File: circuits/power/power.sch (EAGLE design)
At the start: 22 parts

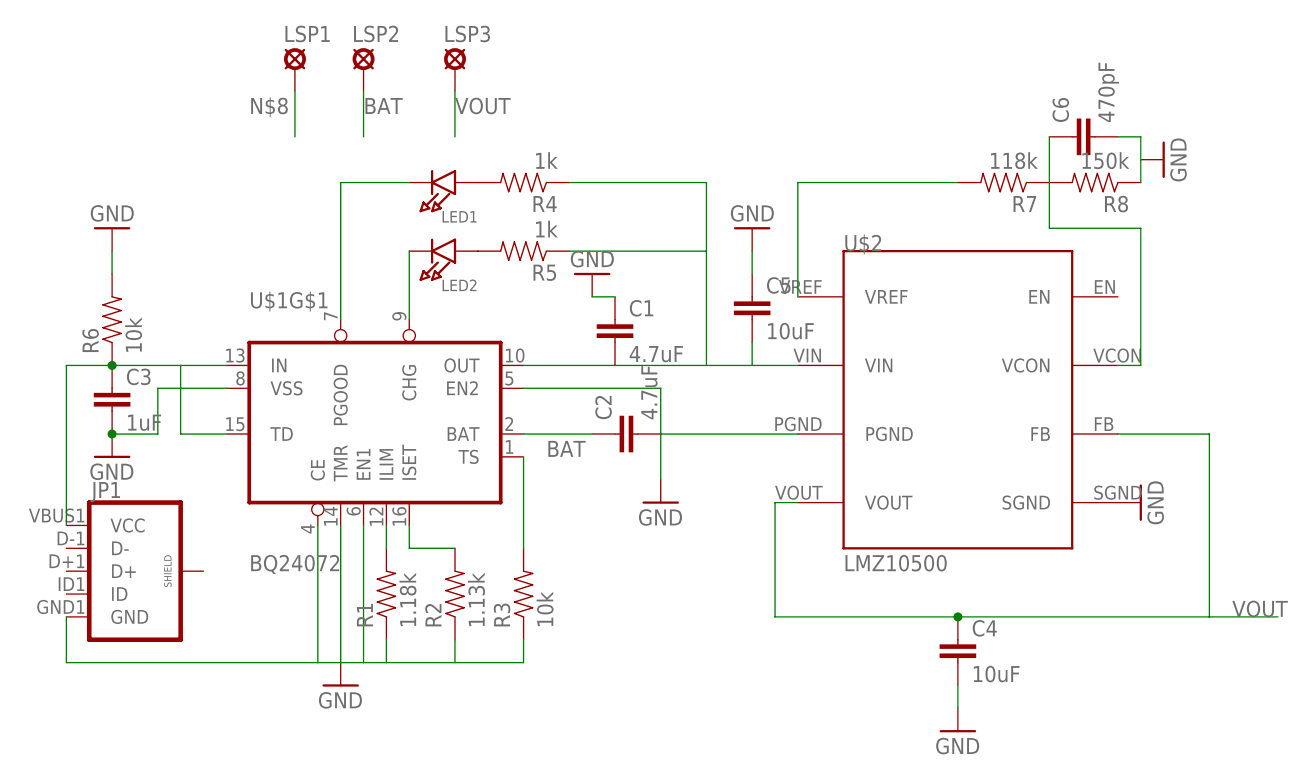
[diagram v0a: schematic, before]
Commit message: changed LMZ10500 library. updated power schematic and switched out usb. Made new power layout.
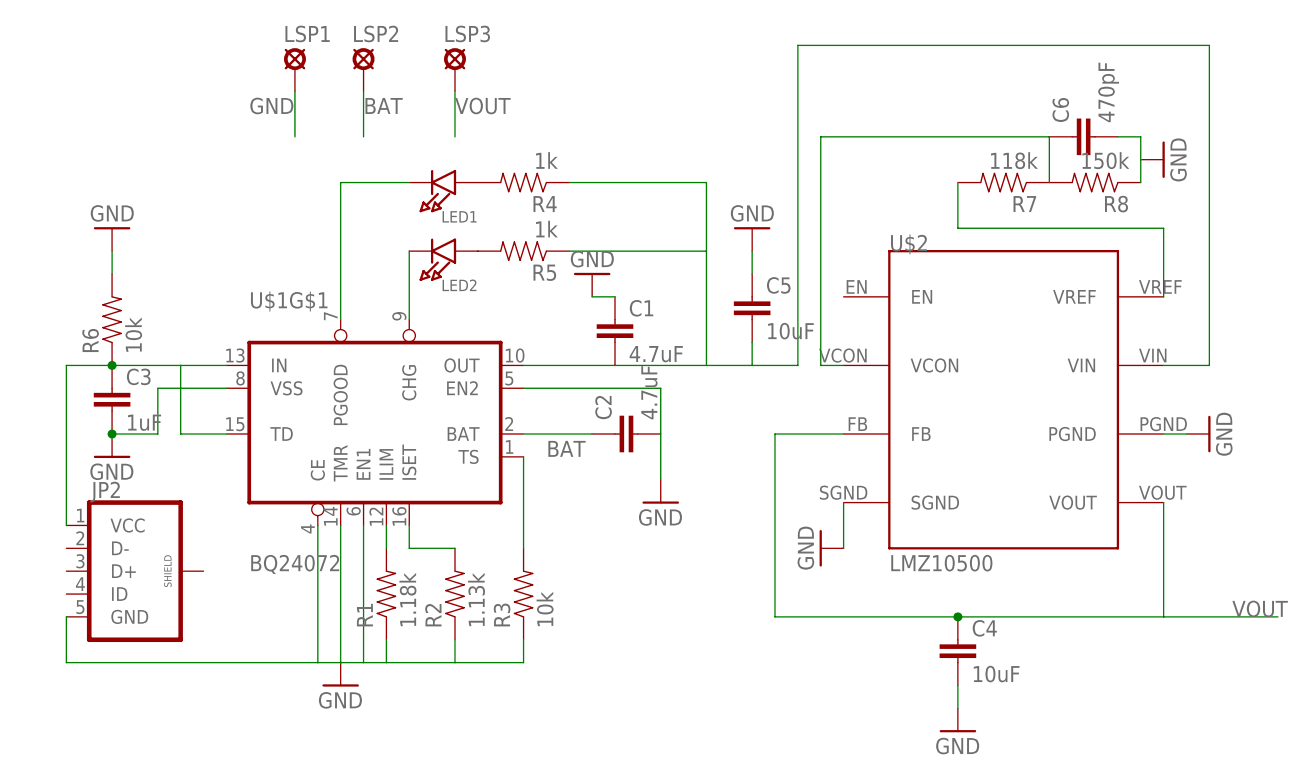
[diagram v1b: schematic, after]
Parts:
- removed JP1: (no value), SparkFun-Connectors:USB_MICROB_PLUGCONN-11752
- added JP2: (no value), SparkFun-Connectors:USB_MICROB_PLUG-SMT
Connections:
- removed net N$25: U$2.SGND
- removed net N$8: C1.1, C2.2, C3.2, C4.2, C5.1, C6.2, JP1.GND, LSP1.MP, R1.1, R2.1, R3.1, R6.2, R8.1, U$1G$1.CE, U$1G$1.EN1, U$1G$1.EN2, U$1G$1.TMR, U$1G$1.VSS, U$2.PGND
- new net GND: C1.1, C2.2, C3.2, C4.2, C5.1, C6.2, JP2.GND, LSP1.MP, R1.1, R2.1, R3.1, R6.2, R8.1, U$1G$1.CE, U$1G$1.EN1, U$1G$1.EN2, U$1G$1.TMR, U$1G$1.VSS, U$2.PGND, U$2.SGND
- net N$14: now also JP2.VCC; no longer JP1.VCC
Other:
- moved on the sheet: U$2
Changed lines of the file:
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@@
 <layer number="112" name="tSilk" color="7" fill="1" visible="yes" active="yes"/>
 <layer number="113" name="IDFDebug" color="4" fill="1" visible="yes" active="yes"/>
+<layer number="114" name="Badge_Outline" color="7" fill="1" visible="yes" active="yes"/>
+<layer number="115" name="ReferenceISLANDS" color="7" fill="1" visible="yes" active="yes"/>
 <layer number="116" name="Patch_BOT" color="9" fill="4" visible="yes" active="yes"/>
 <layer number="118" name="Rect_Pads" color="7" fill="1" visible="yes" active="yes"/>
@@
 <part name="R6" library="SparkFun-Resistors" deviceset="RESISTOR" device="0603" value="10k"/>
 <part name="GND5" library="SparkFun-Aesthetics" deviceset="GND" device=""/>
-<part name="JP1" library="SparkFun-Connectors" deviceset="USB_MICROB_PLUG" device="CONN-11752"/>
 <part name="C4" library="SparkFun-Capacitors" deviceset="CAP" device="0603-CAP" value="10uF"/>
 <part name="C5" library="SparkFun-Capacitors" deviceset="CAP" device="0603-CAP" value="10uF"/>
@@
 <part name="LSP3" library="solpad" deviceset="LSP10" device=""/>
 <part name="U$2" library="LMZ10500" deviceset="LMZ10500" device=""/>
+<part name="GND10" library="SparkFun-Aesthetics" deviceset="GND" device=""/>
+<part name="JP2" library="SparkFun-Connectors" deviceset="USB_MICROB_PLUG" device="-SMT"/>
 </parts>
 <sheets>
@@
 <instance part="R6" gate="G$1" x="63.5" y="63.5" rot="R90"/>
 <instance part="GND5" gate="1" x="63.5" y="73.66" rot="R180"/>
-<instance part="JP1" gate="G$1" x="66.04" y="35.56"/>
 <instance part="C4" gate="G$1" x="157.48" y="25.4"/>
 <instance part="C5" gate="G$1" x="134.62" y="63.5"/>
@@
 <instance part="R7" gate="G$1" x="162.56" y="78.74" rot="R180"/>
 <instance part="R8" gate="G$1" x="172.72" y="78.74" rot="R180"/>
-<instance part="GND6" gate="1" x="177.8" y="43.18" rot="R90"/>
+<instance part="GND6" gate="1" x="142.24" y="38.1" rot="R270"/>
 <instance part="GND7" gate="1" x="134.62" y="73.66" rot="R180"/>
 <instance part="GND8" gate="1" x="157.48" y="17.78"/>
@@
 <instance part="LSP2" gate="1" x="91.44" y="91.44"/>
 <instance part="LSP3" gate="1" x="101.6" y="91.44"/>
-<instance part="U$2" gate="G$1" x="177.8" y="55.88"/>
+<instance part="U$2" gate="G$1" x="182.88" y="55.88"/>
+<instance part="GND10" gate="1" x="185.42" y="50.8" rot="R90"/>
+<instance part="JP2" gate="G$1" x="66.04" y="35.56"/>
 </instances>
 <busses>
 </busses>
 <nets>
-<net name="N$25" class="0">
-<segment>
-<pinref part="GND6" gate="1" pin="GND"/>
-<pinref part="U$2" gate="G$1" pin="SGND"/>
-</segment>
-</net>
 <net name="N$3" class="0">
 <segment>
@@
 <wire x1="129.54" y1="58.42" x2="134.62" y2="58.42" width="0.1524" layer="91"/>
 <pinref part="C5" gate="G$1" pin="2"/>
-<wire x1="134.62" y1="58.42" x2="139.7" y2="58.42" width="0.1524" layer="91"/>
 <wire x1="134.62" y1="60.96" x2="134.62" y2="58.42" width="0.1524" layer="91"/>
 <pinref part="U$2" gate="G$1" pin="VIN"/>
+<wire x1="180.34" y1="58.42" x2="185.42" y2="58.42" width="0.1524" layer="91"/>
+<wire x1="185.42" y1="58.42" x2="185.42" y2="93.98" width="0.1524" layer="91"/>
+<wire x1="185.42" y1="93.98" x2="139.7" y2="93.98" width="0.1524" layer="91"/>
+<wire x1="139.7" y1="93.98" x2="139.7" y2="58.42" width="0.1524" layer="91"/>
+<wire x1="139.7" y1="58.42" x2="134.62" y2="58.42" width="0.1524" layer="91"/>
 </segment>
 </net>
@@
 <pinref part="R6" gate="G$1" pin="1"/>
 <junction x="63.5" y="58.42"/>
-<pinref part="JP1" gate="G$1" pin="VCC"/>
 <wire x1="58.42" y1="40.64" x2="58.42" y2="58.42" width="0.1524" layer="91"/>
 <wire x1="58.42" y1="58.42" x2="63.5" y2="58.42" width="0.1524" layer="91"/>
-</segment>
-</net>
-<net name="N$1" class="0">
-<segment>
-<wire x1="139.7" y1="66.04" x2="139.7" y2="78.74" width="0.1524" layer="91"/>
-<pinref part="R7" gate="G$1" pin="2"/>
-<wire x1="139.7" y1="78.74" x2="157.48" y2="78.74" width="0.1524" layer="91"/>
-<pinref part="U$2" gate="G$1" pin="VREF"/>
+<pinref part="JP2" gate="G$1" pin="VCC"/>
 </segment>
 </net>
 <net name="N$2" class="0">
 <segment>
-<wire x1="175.26" y1="58.42" x2="177.8" y2="58.42" width="0.1524" layer="91"/>
-<wire x1="177.8" y1="58.42" x2="177.8" y2="73.66" width="0.1524" layer="91"/>
 <pinref part="R7" gate="G$1" pin="1"/>
-<wire x1="177.8" y1="73.66" x2="167.64" y2="73.66" width="0.1524" layer="91"/>
-<wire x1="167.64" y1="73.66" x2="167.64" y2="78.74" width="0.1524" layer="91"/>
 <pinref part="R8" gate="G$1" pin="2"/>
 <wire x1="167.64" y1="78.74" x2="167.64" y2="83.82" width="0.1524" layer="91"/>
 <pinref part="C6" gate="G$1" pin="1"/>
 <pinref part="U$2" gate="G$1" pin="VCON"/>
+<wire x1="144.78" y1="58.42" x2="142.24" y2="58.42" width="0.1524" layer="91"/>
+<wire x1="142.24" y1="58.42" x2="142.24" y2="83.82" width="0.1524" layer="91"/>
+<wire x1="142.24" y1="83.82" x2="167.64" y2="83.82" width="0.1524" layer="91"/>
 </segment>
 </net>
 <net name="VOUT" class="0">
 <segment>
-<wire x1="139.7" y1="43.18" x2="137.16" y2="43.18" width="0.1524" layer="91"/>
-<wire x1="137.16" y1="43.18" x2="137.16" y2="30.48" width="0.1524" layer="91"/>
 <wire x1="137.16" y1="30.48" x2="157.48" y2="30.48" width="0.1524" layer="91"/>
-<wire x1="157.48" y1="30.48" x2="185.42" y2="30.48" width="0.1524" layer="91"/>
-<wire x1="185.42" y1="30.48" x2="185.42" y2="50.8" width="0.1524" layer="91"/>
-<wire x1="185.42" y1="50.8" x2="175.26" y2="50.8" width="0.1524" layer="91"/>
 <pinref part="C4" gate="G$1" pin="1"/>
 <junction x="157.48" y="30.48"/>
-<wire x1="185.42" y1="30.48" x2="193.04" y2="30.48" width="0.1524" layer="91"/>
 <label x="187.96" y="30.48" size="1.778" layer="95"/>
 <pinref part="U$2" gate="G$1" pin="VOUT"/>
+<wire x1="180.34" y1="30.48" x2="193.04" y2="30.48" width="0.1524" layer="91"/>
+<wire x1="180.34" y1="30.48" x2="180.34" y2="43.18" width="0.1524" layer="91"/>
 <pinref part="U$2" gate="G$1" pin="FB"/>
+<wire x1="144.78" y1="50.8" x2="137.16" y2="50.8" width="0.1524" layer="91"/>
+<wire x1="137.16" y1="50.8" x2="137.16" y2="30.48" width="0.1524" layer="91"/>
+<wire x1="180.34" y1="30.48" x2="157.48" y2="30.48" width="0.1524" layer="91"/>
 </segment>
 <segment>
@@
 </segment>
 </net>
-<net name="N$8" class="0">
+<net name="GND" class="0">
+<segment>
+<pinref part="U$2" gate="G$1" pin="SGND"/>
+<pinref part="GND6" gate="1" pin="GND"/>
+<wire x1="144.78" y1="38.1" x2="144.78" y2="43.18" width="0.1524" layer="91"/>
+</segment>
+<segment>
+<pinref part="U$2" gate="G$1" pin="PGND"/>
+<pinref part="GND10" gate="1" pin="GND"/>
+<wire x1="182.88" y1="50.8" x2="180.34" y2="50.8" width="0.1524" layer="91"/>
+</segment>
 <segment>
 <pinref part="LSP1" gate="1" pin="MP"/>
@@
 </segment>
 <segment>
-<pinref part="C2" gate="G$1" pin="2"/>
-<pinref part="GND2" gate="1" pin="GND"/>
-<pinref part="U$1" gate="G$1" pin="EN2"/>
-<wire x1="109.22" y1="55.88" x2="124.46" y2="55.88" width="0.1524" layer="91"/>
-<wire x1="124.46" y1="55.88" x2="124.46" y2="50.8" width="0.1524" layer="91"/>
-<wire x1="124.46" y1="50.8" x2="124.46" y2="45.72" width="0.1524" layer="91"/>
-<wire x1="139.7" y1="50.8" x2="124.46" y2="50.8" width="0.1524" layer="91"/>
-<pinref part="U$2" gate="G$1" pin="PGND"/>
+<pinref part="R6" gate="G$1" pin="2"/>
+<pinref part="GND5" gate="1" pin="GND"/>
+<wire x1="63.5" y1="71.12" x2="63.5" y2="68.58" width="0.1524" layer="91"/>
 </segment>
 <segment>
@@
 <wire x1="101.6" y1="25.4" x2="93.98" y2="25.4" width="0.1524" layer="91"/>
 <wire x1="101.6" y1="27.94" x2="101.6" y2="25.4" width="0.1524" layer="91"/>
-<pinref part="JP1" gate="G$1" pin="GND"/>
 <wire x1="58.42" y1="30.48" x2="58.42" y2="25.4" width="0.1524" layer="91"/>
 <wire x1="58.42" y1="25.4" x2="86.36" y2="25.4" width="0.1524" layer="91"/>
+<pinref part="JP2" gate="G$1" pin="GND"/>
 </segment>
 <segment>
@@
 <pinref part="GND9" gate="1" pin="GND"/>
 <wire x1="177.8" y1="81.28" x2="177.8" y2="78.74" width="0.1524" layer="91"/>
-</segment>
-<segment>
-<pinref part="C4" gate="G$1" pin="2"/>
-<pinref part="GND8" gate="1" pin="GND"/>
-<wire x1="157.48" y1="20.32" x2="157.48" y2="22.86" width="0.1524" layer="91"/>
-</segment>
-<segment>
-<pinref part="C5" gate="G$1" pin="1"/>
-<pinref part="GND7" gate="1" pin="GND"/>
-<wire x1="134.62" y1="71.12" x2="134.62" y2="68.58" width="0.1524" layer="91"/>
-</segment>
-<segment>
-<pinref part="C1" gate="G$1" pin="1"/>
-<pinref part="GND3" gate="1" pin="GND"/>
-<wire x1="116.84" y1="66.04" x2="119.38" y2="66.04" width="0.1524" layer="91"/>
-</segment>
-<segment>
-<pinref part="R6" gate="G$1" pin="2"/>
-<pinref part="GND5" gate="1" pin="GND"/>
-<wire x1="63.5" y1="71.12" x2="63.5" y2="68.58" width="0.1524" layer="91"/>
 </segment>
 <segment>
@@
 <junction x="63.5" y="50.8"/>
 </segment>
-</net>
+<segment>
+<pinref part="C1" gate="G$1" pin="1"/>
+<pinref part="GND3" gate="1" pin="GND"/>
+<wire x1="116.84" y1="66.04" x2="119.38" y2="66.04" width="0.1524" layer="91"/>
+</segment>
+<segment>
+<pinref part="C5" gate="G$1" pin="1"/>
+<pinref part="GND7" gate="1" pin="GND"/>
+<wire x1="134.62" y1="71.12" x2="134.62" y2="68.58" width="0.1524" layer="91"/>
+</segment>
+<segment>
+<pinref part="C4" gate="G$1" pin="2"/>
+<pinref part="GND8" gate="1" pin="GND"/>
+<wire x1="157.48" y1="20.32" x2="157.48" y2="22.86" width="0.1524" layer="91"/>
+</segment>
+<segment>
+<pinref part="C2" gate="G$1" pin="2"/>
+<pinref part="GND2" gate="1" pin="GND"/>
+<pinref part="U$1" gate="G$1" pin="EN2"/>
+<wire x1="109.22" y1="55.88" x2="124.46" y2="55.88" width="0.1524" layer="91"/>
+<wire x1="124.46" y1="55.88" x2="124.46" y2="50.8" width="0.1524" layer="91"/>
+<wire x1="124.46" y1="50.8" x2="124.46" y2="45.72" width="0.1524" layer="91"/>
+</segment>
+</net>
+<net name="N$1" class="0">
+<segment>
+<pinref part="R7" gate="G$1" pin="2"/>
+<wire x1="157.48" y1="78.74" x2="157.48" y2="73.66" width="0.1524" layer="91"/>
+<pinref part="U$2" gate="G$1" pin="VREF"/>
+<wire x1="157.48" y1="73.66" x2="180.34" y2="73.66" width="0.1524" layer="91"/>
+<wire x1="180.34" y1="73.66" x2="180.34" y2="66.04" width="0.1524" layer="91"/>
+</segment>
+</net>

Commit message: stuff I dont know
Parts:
- removed C6: 470pF, SparkFun-Capacitors:CAP0603-CAP
- removed R7: 118k, SparkFun-Passives:RESISTOR0603-RES
- removed R8: 150k, SparkFun-Passives:RESISTOR0603-RES
- removed U$2: LMZ10500, LMZ10500:LMZ10500
- added L1: 10uH, SparkFun-Passives:INDUCTOR30OHM,1.8A
- added U$3: TLV61225, tps6122x:TLV61225
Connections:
- removed net N$2: C6.1, R7.1, R8.2, U$2.VCON
- net GND: no longer C6.2, R8.1, U$2.PGND, U$2.SGND
- net N$1: now also L1.2, U$3.L; no longer R7.2, U$2.VREF
- net N$9: now also L1.1, U$3.EN, U$3.VIN; no longer U$2.VIN
- net VOUT: now also U$3.FB, U$3.VOUT; no longer U$2.FB, U$2.VOUT
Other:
- moved on the sheet: C4, C5
